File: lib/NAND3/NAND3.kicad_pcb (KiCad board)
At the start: 2 copper layers, 6 parts

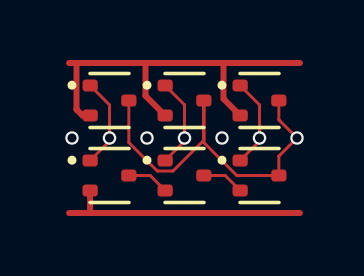
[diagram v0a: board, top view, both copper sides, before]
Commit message: High-density layout with pitch of 1.1mm, which gains 23% !!
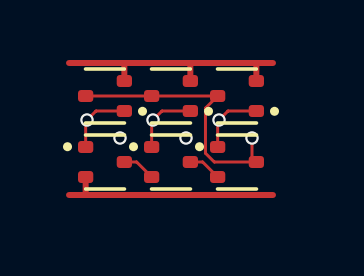
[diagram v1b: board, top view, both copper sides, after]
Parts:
- moved N3 0.87 mm to (5.50, 3.30)
- moved P3 0.76 mm to (5.50, 1.10), turned to 180 degrees
- moved N2 0.64 mm to (3.30, 3.30)
- moved N1 0.47 mm to (1.10, 3.30)
- moved P2 0.47 mm to (3.30, 1.10), turned to 180 degrees
- moved P1 0.21 mm to (1.10, 1.10), turned to 180 degrees
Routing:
- net VDD: track 13.8 -> 8.61 mm
- net Y: track 13.4 -> 9.15 mm
- net GND: track 8.40 -> 7.40 mm
- net C: track 3.03 -> 2.29 mm
- net B: track 3.03 -> 2.29 mm
- net A: track 3.03 -> 2.29 mm
- net (no net): vias 3 -> 2

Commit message: NAND3: rename inputs A1, A2, A3
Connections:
- net A renamed A1
- net B renamed A2
- net C renamed A3
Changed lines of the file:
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@@
 	(net 1 "GND")
 	(net 2 "Y")
-	(net 3 "C")
+	(net 3 "A3")
 	(net 4 "VDD")
-	(net 5 "A")
-	(net 6 "B")
+	(net 5 "A1")
+	(net 6 "A2")
 	(net 7 "int1")
 	(net 8 "int2")
@@
 			(layers "F.Cu" "F.Mask" "F.Paste")
 			(roundrect_rratio 0.25)
-			(net 3 "C")
+			(net 3 "A3")
 			(pinfunction "G")
 			(pintype "inout")
@@
 			(layers "F.Cu" "F.Mask" "F.Paste")
 			(roundrect_rratio 0.25)
-			(net 5 "A")
+			(net 5 "A1")
 			(pinfunction "G")
 			(pintype "inout")
@@
 			(layers "F.Cu" "F.Mask" "F.Paste")
 			(roundrect_rratio 0.25)
-			(net 3 "C")
+			(net 3 "A3")
 			(pinfunction "G")
 			(pintype "inout")
@@
 			(layers "F.Cu" "F.Mask" "F.Paste")
 			(roundrect_rratio 0.25)
-			(net 6 "B")
+			(net 6 "A2")
 			(pinfunction "G")
 			(pintype "inout")
@@
 			(layers "F.Cu" "F.Mask" "F.Paste")
 			(roundrect_rratio 0.25)
-			(net 6 "B")
+			(net 6 "A2")
 			(pinfunction "G")
 			(pintype "inout")
@@
 			(layers "F.Cu" "F.Mask" "F.Paste")
 			(roundrect_rratio 0.25)
-			(net 5 "A")
+			(net 5 "A1")
 			(pinfunction "G")
 			(pintype "inout")

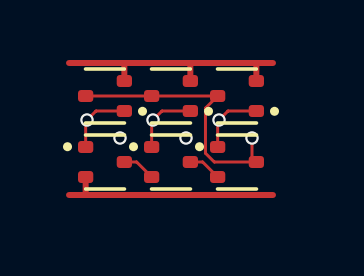
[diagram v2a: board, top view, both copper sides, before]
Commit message: All cells now use 1mm*4mm grid rather than 1.1mm*4.4mm
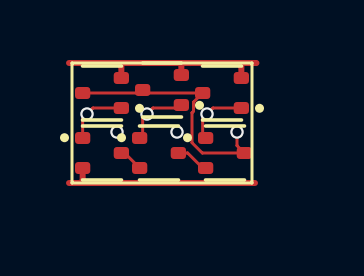
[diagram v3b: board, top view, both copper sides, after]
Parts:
- moved P3 0.51 mm to (5.00, 1.00)
- moved N3 0.50 mm to (5.10, 3.00)
- moved N2 0.50 mm to (2.90, 3.00)
- moved P2 0.36 mm to (3.00, 0.90)
- moved N1 0.32 mm to (1.00, 3.00)
- moved P1 0.14 mm to (1.00, 1.00)
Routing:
- net VDD: track 8.61 -> 7.78 mm
- net Y: track 9.15 -> 8.49 mm
- net GND: track 7.40 -> 6.74 mm
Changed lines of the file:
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@@
 	(footprint "Package_TO_SOT_SMD:SOT-523"
 		(layer "F.Cu")
-		(at 5.5 1.1 180)
+		(at 5 1 180)
 		(descr "SOT523, https://www.diodes.com/assets/Package-Files/SOT523.pdf")
 		(tags "SOT-523")
@@
 	(footprint "Package_TO_SOT_SMD:SOT-523"
 		(layer "F.Cu")
-		(at 1.1 1.1 180)
+		(at 1 1 180)
 		(descr "SOT523, https://www.diodes.com/assets/Package-Files/SOT523.pdf")
 		(tags "SOT-523")
@@
 	(footprint "Package_TO_SOT_SMD:SOT-523"
 		(layer "F.Cu")
-		(at 5.5 3.3)
+		(at 5.1 3)
 		(descr "SOT523, https://www.diodes.com/assets/Package-Files/SOT523.pdf")
 		(tags "SOT-523")
@@
 	(footprint "Package_TO_SOT_SMD:SOT-523"
 		(layer "F.Cu")
-		(at 3.3 1.1 180)
+		(at 3 0.9 180)
 		(descr "SOT523, https://www.diodes.com/assets/Package-Files/SOT523.pdf")
 		(tags "SOT-523")
@@
 	(footprint "Package_TO_SOT_SMD:SOT-523"
 		(layer "F.Cu")
-		(at 3.3 3.3)
+		(at 2.9 3)
 		(descr "SOT523, https://www.diodes.com/assets/Package-Files/SOT523.pdf")
 		(tags "SOT-523")
@@
 	(footprint "Package_TO_SOT_SMD:SOT-523"
 		(layer "F.Cu")
-		(at 1.1 3.3)
+		(at 1 3)
 		(descr "SOT523, https://www.diodes.com/assets/Package-Files/SOT523.pdf")
 		(tags "SOT-523")
@@
 		)
 	)
+	(gr_rect
+		(start 0 0)
+		(end 6 4)
+		(stroke
+			(width 0.1)
+			(type default)
+		)
+		(fill no)
+		(layer "F.SilkS")
+	)
 	(via
-		(at 3.8 2.5)
+		(at 3.5 2.3)
 		(size 0.45)
 		(drill 0.3)
@@
 	)
 	(via
-		(at 1.6 2.5)
+		(at 1.5 2.3)
 		(size 0.45)
 		(drill 0.3)
@@
 	)
 	(segment
-		(start -0.1 4.4)
-		(end 0.45 4.4)
+		(start -0.1 4)
+		(end 0.45 4)
 		(width 0.2)
 		(layer "F.Cu")
@@
 	)
 	(segment
-		(start 0.455 4.395)
-		(end 0.45 4.4)
+		(start 0.355 3.5)
+		(end 0.355 3.905)
 		(width 0.2)
 		(layer "F.Cu")
@@
 	)
 	(segment
-		(start 0.45 4.4)
-		(end 6.7 4.4)
+		(start 0.355 3.905)
+		(end 0.45 4)
 		(width 0.2)
 		(layer "F.Cu")
@@
 	)
 	(segment
-		(start 0.455 3.8)
-		(end 0.455 4.395)
+		(start 0.455 4)
+		(end 0.45 4)
 		(width 0.2)
 		(layer "F.Cu")
@@
 	)
 	(segment
-		(start 6 3.155)
-		(end 6.145 3.3)
+		(start 0.45 4)
+		(end 6.1 4)
+		(width 0.2)
+		(layer "F.Cu")
+		(net 1)
+	)
+	(segment
+		(start 5.5 2.3)
+		(end 5.5 2.755)
 		(width 0.1)
 		(layer "F.Cu")
@@
 	)
 	(segment
-		(start 4.855 1.1)
-		(end 4.449 1.506)
+		(start 4.342262 3)
+		(end 4 2.657738)
 		(width 0.1)
 		(layer "F.Cu")
@@
 	)
 	(segment
-		(start 6 2.5)
-		(end 6 3.155)
+		(start 5.5 2.755)
+		(end 5.745 3)
 		(width 0.1)
 		(layer "F.Cu")
@@
 	)
 	(segment
-		(start 2.655 1.1)
-		(end 4.855 1.1)
+		(start 4 1.657738)
+		(end 4.051 1.606738)
 		(width 0.1)
 		(layer "F.Cu")
@@
 	)
 	(segment
-		(start 0.455 1.1)
-		(end 2.655 1.1)
+		(start 4.051 1.304)
+		(end 4.355 1)
 		(width 0.1)
 		(layer "F.Cu")
@@
 	)
 	(segment
-		(start 4.449 1.506)
-		(end 4.449 3.006738)
+		(start 2.355 1)
+		(end 4.355 1)
 		(width 0.1)
 		(layer "F.Cu")
@@
 	)
 	(segment
-		(start 4.449 3.006738)
-		(end 4.742262 3.3)
+		(start 4.051 1.606738)
+		(end 4.051 1.304)
 		(width 0.1)
 		(layer "F.Cu")
@@
 	)
 	(segment
-		(start 4.742262 3.3)
-		(end 6.145 3.3)
+		(start 0.355 1)
+		(end 2.355 1)
 		(width 0.1)
 		(layer "F.Cu")
 		(net 2)
 	)
+	(segment
+		(start 4 2.657738)
+		(end 4 1.657738)
+		(width 0.1)
+		(layer "F.Cu")
+		(net 2)
+	)
+	(segment
+		(start 5.745 3)
+		(end 4.342262 3)
+		(width 0.1)
+		(layer "F.Cu")
+		(net 2)
+	)
 	(via
-		(at 6 2.5)
+		(at 5.5 2.3)
 		(size 0.45)
 		(drill 0.3)
@@
 	)
 	(segment
-		(start 4.855 1.945)
-		(end 4.9 1.9)
+		(start 4.7 1.5)
+		(end 4.5 1.7)
 		(width 0.1)
 		(layer "F.Cu")
@@
 	)
 	(segment
-		(start 6.145 1.6)
-		(end 5.2 1.6)
+		(start 5.645 1.5)
+		(end 4.7 1.5)
 		(width 0.1)
 		(layer "F.Cu")
@@
 	)
 	(segment
-		(start 4.855 2.8)
-		(end 4.855 1.945)
+		(start 4.355 1.845)
+		(end 4.5 1.7)
 		(width 0.1)
 		(layer "F.Cu")
@@
 	)
 	(segment
-		(start 5.2 1.6)
-		(end 4.9 1.9)
+		(start 4.355 2.5)
+		(end 4.355 1.845)
 		(width 0.1)
 		(layer "F.Cu")
@@
 	)
 	(via
-		(at 4.9 1.9)
+		(at 4.5 1.7)
 		(size 0.45)
 		(drill 0.3)
@@
 	)
 	(segment
+		(start 1.645 0.045)
+		(end 1.6 0)
+		(width 0.2)
+		(layer "F.Cu")
+		(net 4)
+	)
+	(segment
+		(start 3.645 0.5)
+		(end 3.645 0.045)
+		(width 0.2)
+		(layer "F.Cu")
+		(net 4)
+	)
+	(segment
 		(start 3.945 0.005)
 		(end 3.95 0)
@@
 	(segment
 		(start 1.75 0)
-		(end 3.95 0)
+		(end 3.6 0)
 		(width 0.2)
 		(layer "F.Cu")
@@
 	)
 	(segment
-		(start 3.945 0.6)
-		(end 3.945 0.005)
+		(start 1.6 0)
+		(end 1.75 0)
 		(width 0.2)
 		(layer "F.Cu")
@@
 	)
 	(segment
+		(start 5.6 0)
+		(end 6.1 0)
+		(width 0.2)
+		(layer "F.Cu")
+		(net 4)
+	)
+	(segment
 		(start 3.95 0)
-		(end 6.15 0)
+		(end 5.6 0)
+		(width 0.2)
+		(layer "F.Cu")
+		(net 4)
+	)
+	(segment
+		(start 3.645 0.045)
+		(end 3.6 0)
+		(width 0.2)
+		(layer "F.Cu")
+		(net 4)
+	)
+	(segment
+		(start 1.645 0.5)
+		(end 1.645 0.045)
 		(width 0.2)
 		(layer "F.Cu")
@@
 	(segment
 		(start -0.1 0)
-		(end 1.75 0)
+		(end 1.6 0)
 		(width 0.2)
 		(layer "F.Cu")
@@
 	)
 	(segment
-		(start 6.145 0.6)
-		(end 6.145 0.005)
-		(width 0.2)
-		(layer "F.Cu")
-		(net 4)
-	)
-	(segment
-		(start 6.15 0)
-		(end 6.7 0)
+		(start 3.6 0)
+		(end 3.95 0)
 		(width 0.2)
 		(layer "F.Cu")
@@
 	)
 	(segment
-		(start 1.745 0.6)
-		(end 1.745 0.005)
+		(start 5.645 0.5)
+		(end 5.645 0.045)
 		(width 0.2)
 		(layer "F.Cu")
@@
 	)
 	(segment
-		(start 0.8 1.6)
-		(end 0.5 1.9)
+		(start 5.645 0.045)
+		(end 5.6 0)
+		(width 0.2)
+		(layer "F.Cu")
+		(net 4)
+	)
+	(segment
+		(start 1.645 1.5)
+		(end 0.7 1.5)
 		(width 0.1)
 		(layer "F.Cu")
@@
 	)
 	(segment
-		(start 1.745 1.6)
-		(end 0.8 1.6)
+		(start 0.355 2.5)
+		(end 0.355 1.845)
 		(width 0.1)
 		(layer "F.Cu")
@@
 	)
 	(segment
-		(start 0.455 2.8)
-		(end 0.455 1.945)
+		(start 0.355 1.845)
+		(end 0.5 1.7)
 		(width 0.1)
 		(layer "F.Cu")
@@
 	)
 	(segment
-		(start 0.455 1.945)
-		(end 0.5 1.9)
+		(start 0.7 1.5)
+		(end 0.5 1.7)
 		(width 0.1)
 		(layer "F.Cu")
@@
 	)
 	(via
-		(at 0.5 1.9)
+		(at 0.5 1.7)
 		(size 0.45)
 		(drill 0.3)
@@
 	)
 	(segment
-		(start 3 1.6)
-		(end 2.7 1.9)
+		(start 3.645 1.5)
+		(end 2.7 1.5)
 		(width 0.1)
 		(layer "F.Cu")
@@
 	)
 	(segment
-		(start 2.655 1.945)
-		(end 2.7 1.9)
+		(start 2.355 1.845)
+		(end 2.5 1.7)
 		(width 0.1)
 		(layer "F.Cu")
@@
 	)
 	(segment
-		(start 2.655 2.8)
-		(end 2.655 1.945)
+		(start 2.7 1.5)
+		(end 2.5 1.7)
 		(width 0.1)
 		(layer "F.Cu")
@@
 	)
 	(segment
-		(start 3.945 1.6)
-		(end 3 1.6)
+		(start 2.355 2.5)
+		(end 2.355 1.845)
 		(width 0.1)
 		(layer "F.Cu")
@@
 	)
 	(via
-		(at 2.7 1.9)
+		(at 2.5 1.7)
 		(size 0.45)
 		(drill 0.3)
@@
 	)
 	(segment
-		(start 1.745 3.3)
-		(end 2.155 3.3)
+		(start 1.755 3)
+		(end 2.255 3.5)
 		(width 0.1)
 		(layer "F.Cu")
@@
 	)
 	(segment
-		(start 2.155 3.3)
-		(end 2.655 3.8)
+		(start 1.645 3)
+		(end 1.755 3)
 		(width 0.1)
 		(layer "F.Cu")
@@
 	)
 	(segment
-		(start 4.355 3.3)
-		(end 4.855 3.8)
+		(start 3.855 3)
+		(end 4.355 3.5)
 		(width 0.1)
 		(layer "F.Cu")
@@
 	)
 	(segment
-		(start 3.945 3.3)
-		(end 4.355 3.3)
-		(width 0.1)
-		(layer "F.Cu")
+		(start 3.545 3)
+		(end 3.855 3)
+		(width 0.1)
+		(layer "F.Cu")

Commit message: Make the pads of my SOT523 footprint very slightly smaller, which is enough to route all the cells and leave the mosfets exactly on the grid
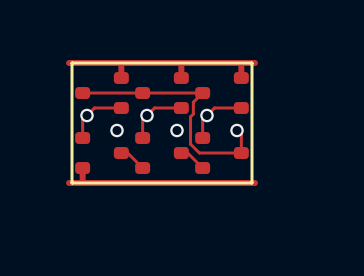
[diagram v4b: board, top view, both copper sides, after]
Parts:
- N1, N2, N3, P1, P2, P3: footprint Package_TO_SOT_SMD:SOT-523 -> RV523:SOT523
- moved N2 0.10 mm to (3.00, 3.00)
- moved P2 0.10 mm to (3.00, 1.00)
- moved N3 0.10 mm to (5.00, 3.00)

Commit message: Propagate MOSFET values to the cells' PCBs
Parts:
- N1, N2, N3: value (none) -> NMOS
- P1, P2, P3: value (none) -> PMOS
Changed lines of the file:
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@@
 			)
 		)
-		(property "Value" ""
+		(property "Value" "PMOS"
 			(at 0 0 180)
 			(layer "F.Fab")
@@
 			)
 		)
-		(property "Value" ""
+		(property "Value" "PMOS"
 			(at 0 0 180)
 			(layer "F.Fab")
@@
 			)
 		)
-		(property "Value" ""
+		(property "Value" "NMOS"
 			(at 0 0 0)
 			(layer "F.Fab")
@@
 			)
 		)
-		(property "Value" ""
+		(property "Value" "PMOS"
 			(at 0 0 180)
 			(layer "F.Fab")
@@
 			)
 		)
-		(property "Value" ""
+		(property "Value" "NMOS"
 			(at 0 0 0)
 			(layer "F.Fab")
@@
 			)
 		)
-		(property "Value" ""
-			(at 0 0 0)
-			(layer "F.Fab")
+		(property "Value" "NMOS"
+			(at 0 0 0)
+			(layer "F.Fab")
